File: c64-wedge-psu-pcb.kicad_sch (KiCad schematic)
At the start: 22 parts, among them U1 LM2576T-ADJ

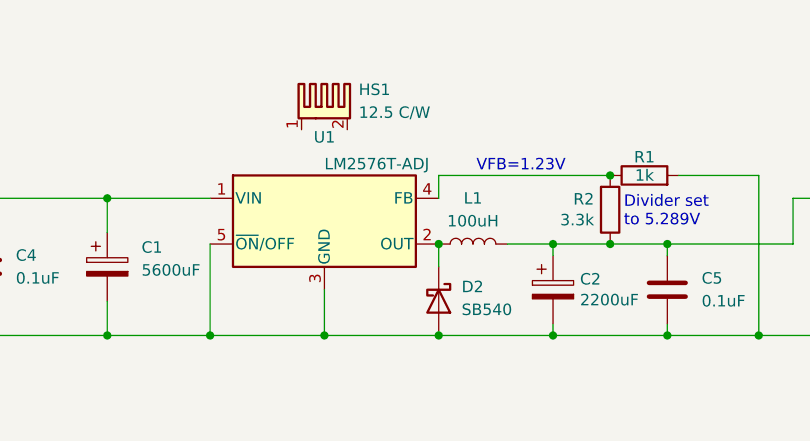
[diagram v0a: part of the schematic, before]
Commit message: created 3D model for heatsink + moved bridge rectifier + version number on PCB = 2.1.0
Changed heatsink to ATS-PCB1035 after measuring physical example and creating 3D model and footprint for it
Moved bridge rectifier after finding and fixing error in its KiCad 3D model
Changed version number on PCB to 2.1.0
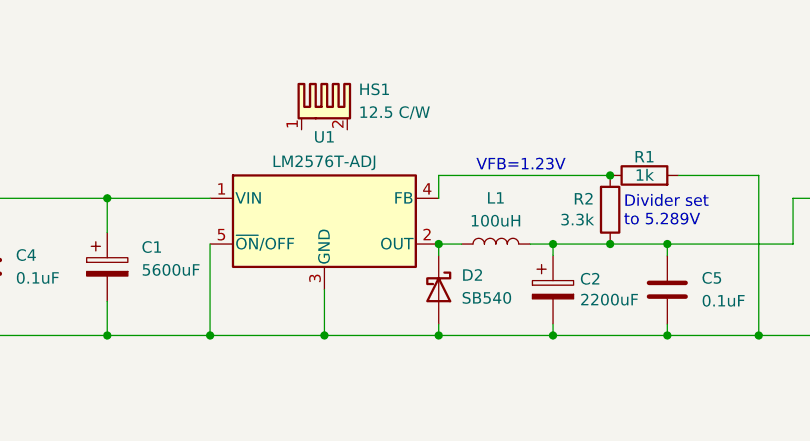
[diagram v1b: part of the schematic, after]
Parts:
- HS1: footprint c64-wedge-psu-pcb:ATS-PCB1036 -> c64-wedge-psu-pcb:ATS-PCB1035
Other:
- moved on the sheet: D2, L1
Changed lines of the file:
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@@
 	(wire
 		(pts
-			(xy 137.16 97.79) (xy 142.24 97.79)
+			(xy 139.7 97.79) (xy 142.24 97.79)
 		)
 		(stroke
@@
 	(wire
 		(pts
+			(xy 129.54 106.68) (xy 129.54 107.95)
+		)
+		(stroke
+			(width 0)
+			(type default)
+		)
+	)
+	(wire
+		(pts
+			(xy 132.08 97.79) (xy 129.54 97.79)
+		)
+		(stroke
+			(width 0)
+			(type default)
+		)
+	)
+	(wire
+		(pts
 			(xy 64.77 100.33) (xy 64.77 111.76)
 		)
@@
 	(wire
 		(pts
-			(xy 129.54 97.79) (xy 129.54 100.33)
+			(xy 129.54 97.79) (xy 129.54 99.06)
 		)
 		(stroke
@@
 		)
 		(property "Value" "LM2576T-ADJ"
-			(at 116.84 88.9 0)
-			(effects
-				(font
-					(size 1.27 1.27)
-				)
-				(justify left)
+			(at 116.84 88.646 0)
+			(effects
+				(font
+					(size 1.27 1.27)
+				)
 			)
 		)
@@
 	(symbol
 		(lib_id "Device:L")
-		(at 133.35 97.79 90)
+		(at 135.89 97.79 90)
 		(unit 1)
 		(exclude_from_sim no)
@@
 		(fields_autoplaced yes)
 		(property "Reference" "L1"
-			(at 133.35 92.71 90)
+			(at 135.89 92.71 90)
 			(effects
 				(font
@@
 		)
 		(property "Value" "100uH"
-			(at 133.35 95.25 90)
+			(at 135.89 95.25 90)
 			(effects
 				(font
@@
 		)
 		(property "Footprint" "Inductor_THT:L_Toroid_Vertical_L24.6mm_W15.5mm_P11.44mm_Pulse_KM-4"
-			(at 133.35 97.79 0)
+			(at 135.89 97.79 0)
 			(effects
 				(font
@@
 		)
 		(property "Datasheet" "https://yageogroup.com/content/datasheet/asset/file/DATASHEET_P596"
-			(at 133.35 97.79 0)
+			(at 135.89 97.79 0)
 			(effects
 				(font
@@
 		)
 		(property "Description" "Pulse PE-92108KNL (100µH, KM-4)"
-			(at 133.35 97.79 0)
+			(at 135.89 97.79 0)
 			(effects
 				(font
@@
 	(symbol
 		(lib_id "Device:D_Schottky")
-		(at 129.54 104.14 270)
+		(at 129.54 102.87 270)
 		(unit 1)
 		(exclude_from_sim no)
@@
 		(fields_autoplaced yes)
 		(property "Reference" "D2"
-			(at 132.08 102.5524 90)
+			(at 132.08 101.2824 90)
 			(effects
 				(font
@@
 		)
 		(property "Value" "SB540"
-			(at 132.08 105.0924 90)
+			(at 132.08 103.8224 90)
 			(effects
 				(font
@@
 		)
 		(property "Footprint" "Diode_THT:D_DO-201AD_P12.70mm_Horizontal"
-			(at 129.54 104.14 0)
+			(at 129.54 102.87 0)
 			(effects
 				(font
@@
 		)
 		(property "Datasheet" "~"
-			(at 129.54 104.14 0)
+			(at 129.54 102.87 0)
 			(effects
 				(font
@@
 		)
 		(property "Description" "SB540-E3/54"
-			(at 129.54 104.14 0)
+			(at 129.54 102.87 0)
 			(effects
 				(font
@@
 			)
 		)
-		(property "Footprint" "c64-wedge-psu-pcb:ATS-PCB1036"
+		(property "Footprint" "c64-wedge-psu-pcb:ATS-PCB1035"
 			(at 117.1448 83.82 0)
 			(effects
